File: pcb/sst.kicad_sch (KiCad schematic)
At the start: 24 parts

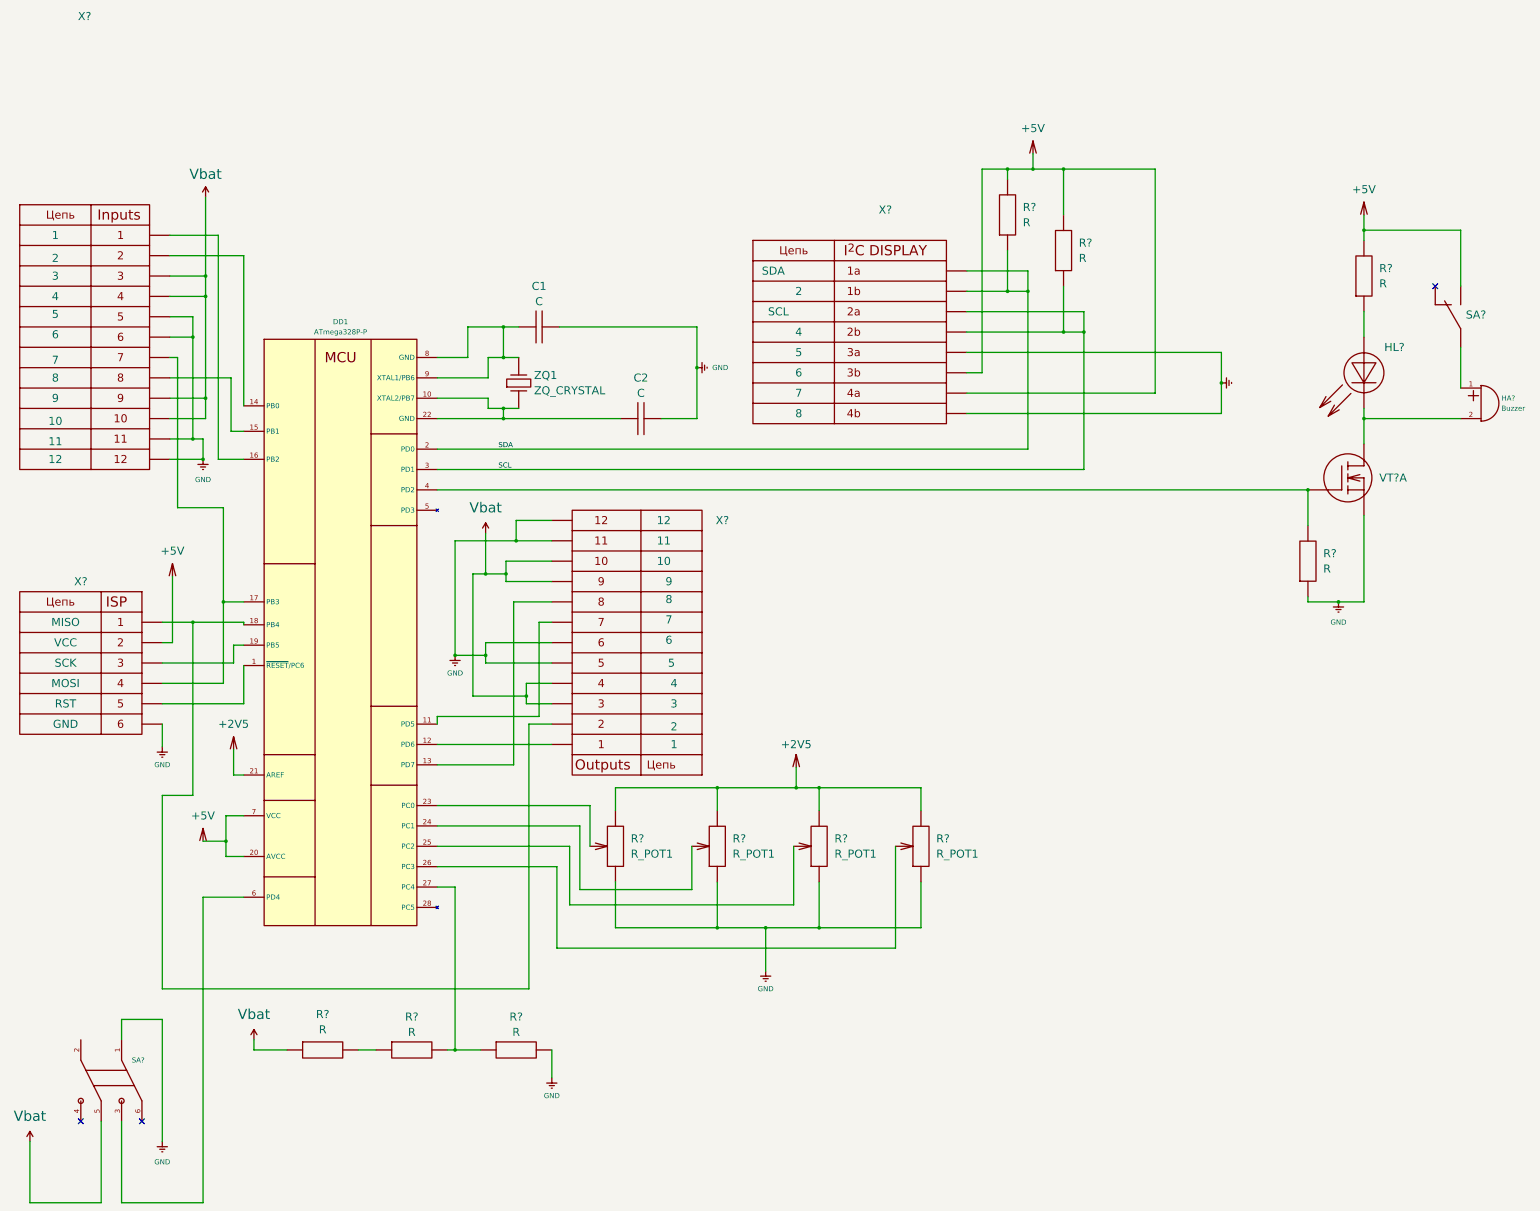
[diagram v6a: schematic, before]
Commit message: надпись «контакты» на уго
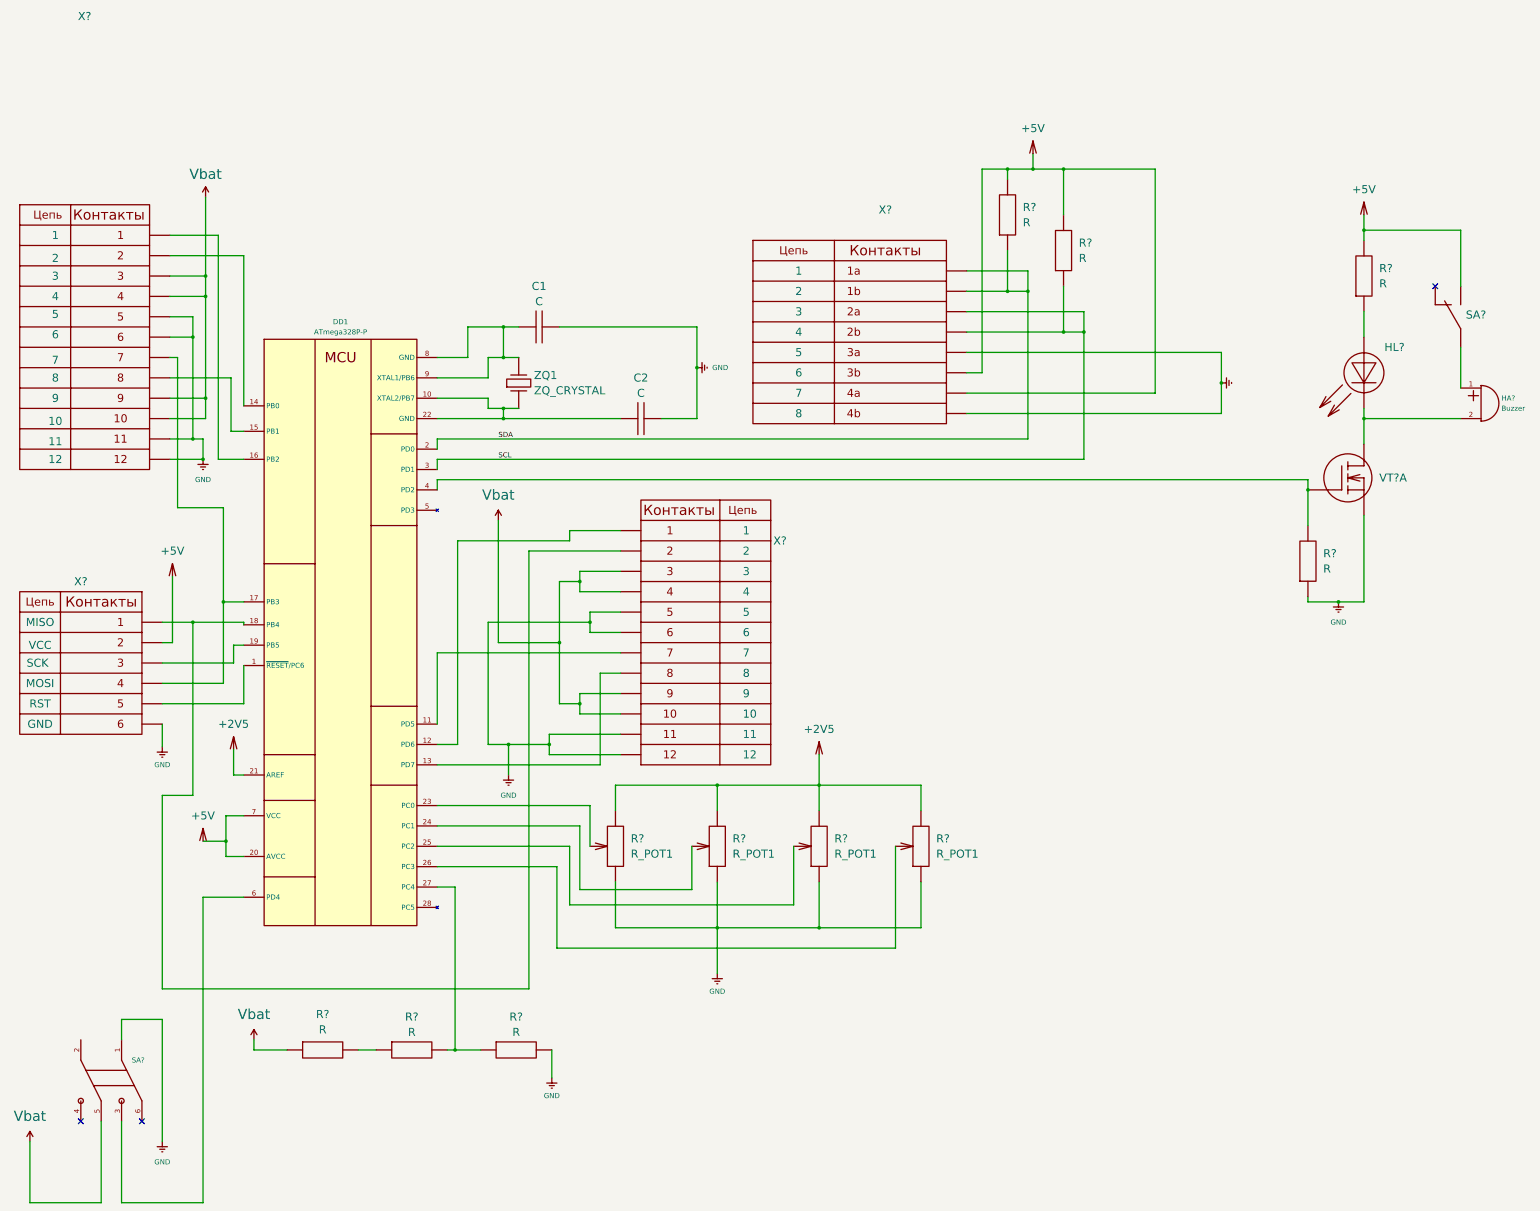
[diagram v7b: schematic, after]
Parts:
- removed X?: CONN_INPUTS, symbol sst:CONN_OUTPUTS
- added X?: CONN_INPUTS, symbol sst:CONN_OUTPUTS
- X?: PIN1 SDA -> 1; PIN3 SCL -> 3
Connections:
- net GND: now also X?.11, X?.12, X?.5, X?.6
- net Vbat: now also X?.10, X?.3, X?.4, X?.9
- net at DD1.11 (PD5): now also X?.7
- net at DD1.12 (PD6): now also X?.1
- net at DD1.13 (PD7): now also X?.8
- net at DD1.18 (PB4), X?.1: now also X?.2
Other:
- moved on the sheet: X?

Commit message: Символ земли без Value "GND"
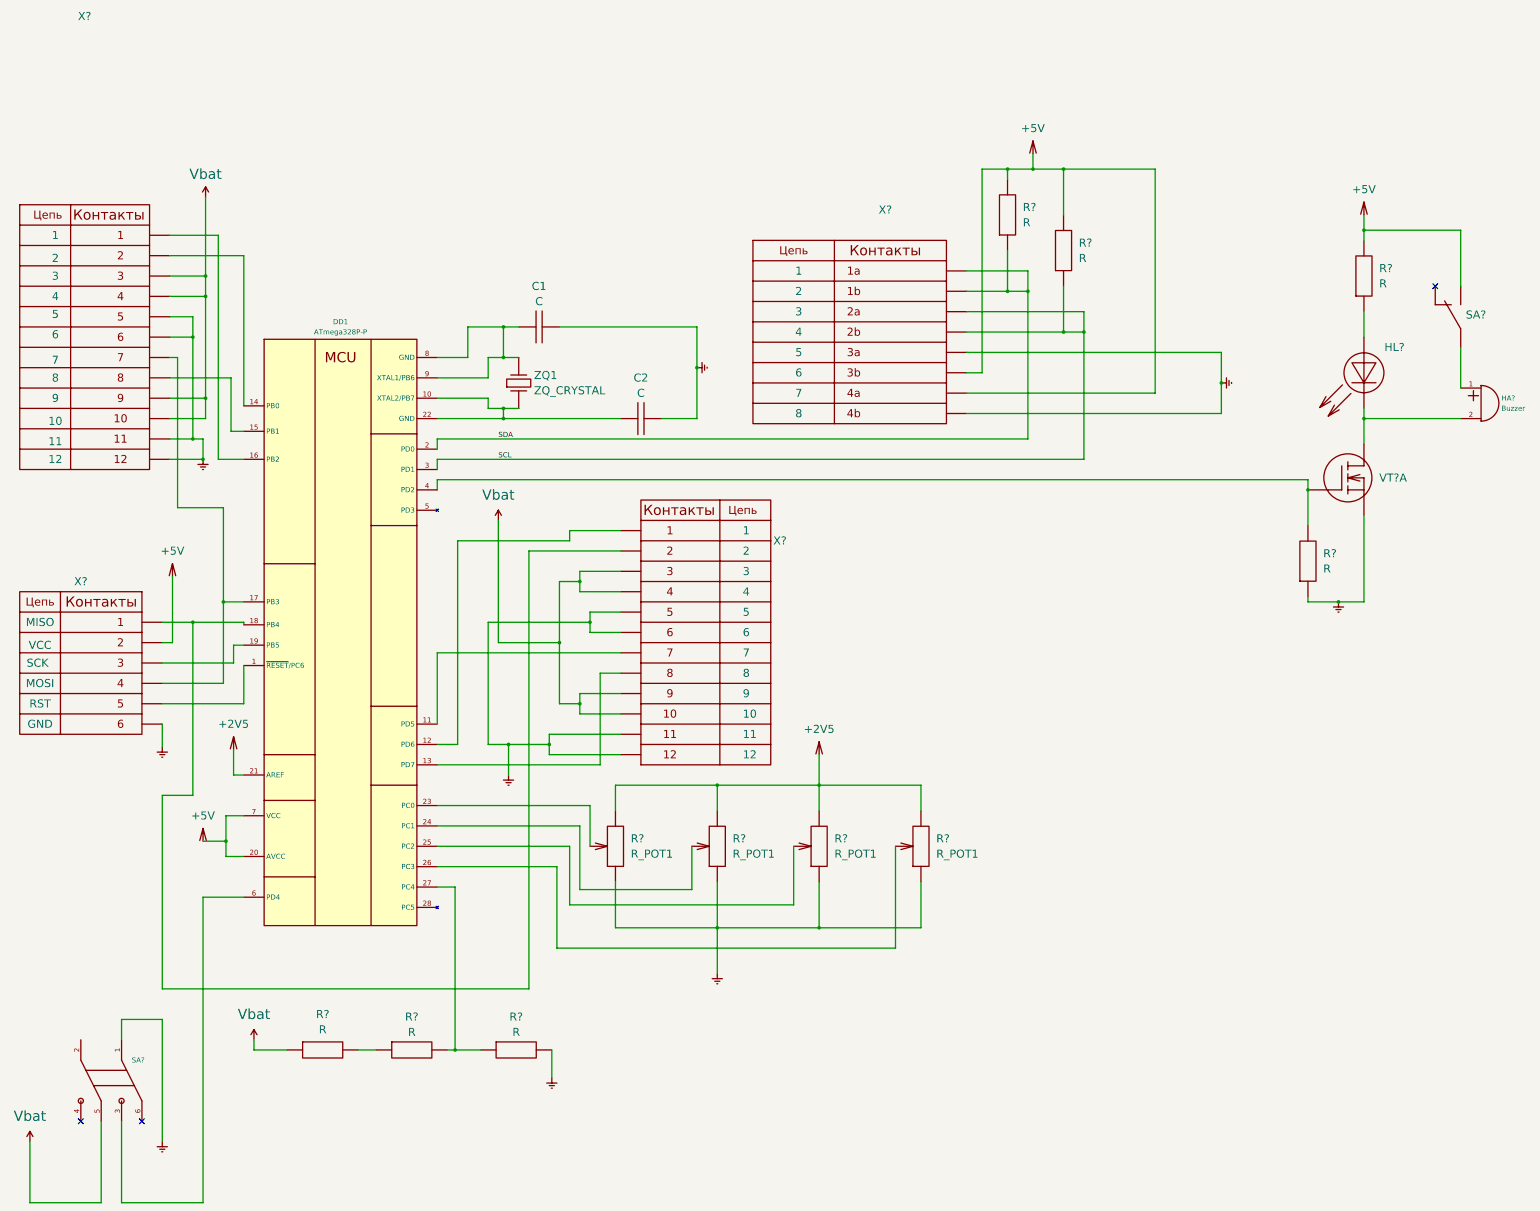
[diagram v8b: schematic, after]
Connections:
- removed net GND: C1.2, C2.1, R?.1, R?.1, R?.1, R?.1, R?.1, R?.2, SA?.1, VT?.1 (S1), X?.11, X?.11, X?.12, X?.12, X?.5, X?.5, X?.5, X?.6, X?.6, X?.6, X?.8
- new net: R?.1, R?.1, R?.1, R?.1
- new net: X?.11, X?.12, X?.5, X?.6 (x2)
- new net: X?.5, X?.8
- new net: C1.2, C2.1
- new net: R?.1, VT?.1 (S1)
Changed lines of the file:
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@@
 		(dnp no)
 		(fields_autoplaced yes)
-		(property "Reference" "#PWR015"
+		(property "Reference" "#PWR15"
 			(at 149.86 179.07 0)
 			(effects
@@
 			)
 		)
-		(property "Value" "GND"
-			(at 149.86 177.8 0)
+		(property "Value" ""
+			(at 149.86 176.53 0)
 			(effects
 				(font
@@
 			(project ""
 				(path "/d486a0a8-b0b2-426a-9635-bf463f56fa2d"
-					(reference "#PWR015")
+					(reference "#PWR15")
 					(unit 1)
 				)
@@
 		(dnp no)
 		(fields_autoplaced yes)
-		(property "Reference" "#PWR09"
+		(property "Reference" "#PWR9"
 			(at 73.66 100.33 0)
 			(effects
@@
 			)
 		)
-		(property "Value" "GND"
-			(at 73.66 99.06 0)
+		(property "Value" ""
+			(at 73.66 97.79 0)
 			(effects
 				(font
@@
 			(project ""
 				(path "/d486a0a8-b0b2-426a-9635-bf463f56fa2d"
-					(reference "#PWR09")
+					(reference "#PWR9")
 					(unit 1)
 				)
@@
 		(dnp no)
 		(fields_autoplaced yes)
-		(property "Reference" "#PWR01"
+		(property "Reference" "#PWR1"
 			(at 203.2 71.12 0)
 			(effects
@@
 			)
 		)
-		(property "Value" "GND"
-			(at 200.66 71.1199 90)
+		(property "Value" ""
+			(at 200.66 71.12 0)
 			(effects
 				(font
 					(size 1.27 1.27)
 				)
-				(justify right)
 			)
 		)
@@
 			(project ""
 				(path "/d486a0a8-b0b2-426a-9635-bf463f56fa2d"
-					(reference "#PWR01")
+					(reference "#PWR1")
 					(unit 1)
 				)
@@
 		(dnp no)
 		(fields_autoplaced yes)
-		(property "Reference" "#PWR07"
+		(property "Reference" "#PWR7"
 			(at 63.5 172.085 0)
 			(effects
@@
 			)
 		)
-		(property "Value" "GND"
-			(at 63.5 170.18 0)
+		(property "Value" ""
+			(at 63.5 169.545 0)
 			(effects
 				(font
@@
 			(project ""
 				(path "/d486a0a8-b0b2-426a-9635-bf463f56fa2d"
-					(reference "#PWR07")
+					(reference "#PWR7")
 					(unit 1)
 				)
@@
 		(dnp no)
 		(fields_autoplaced yes)
-		(property "Reference" "#PWR02"
+		(property "Reference" "#PWR2"
 			(at 334.01 74.93 0)
 			(effects
@@
 			)
 		)
-		(property "Value" "GND"
-			(at 331.47 74.9299 90)
+		(property "Value" ""
+			(at 331.47 74.93 0)
 			(effects
 				(font
 					(size 1.27 1.27)
 				)
-				(justify right)
-				(hide yes)
 			)
 		)
@@
 			(project ""
 				(path "/d486a0a8-b0b2-426a-9635-bf463f56fa2d"
-					(reference "#PWR02")
+					(reference "#PWR2")
 					(unit 1)
 				)
@@
 		(dnp no)
 		(fields_autoplaced yes)
-		(property "Reference" "#PWR04"
+		(property "Reference" "#PWR4"
 			(at 356.87 135.89 0)
 			(effects
@@
 			)
 		)
-		(property "Value" "GND"
-			(at 356.87 134.62 0)
+		(property "Value" ""
+			(at 356.87 133.35 0)
 			(effects
 				(font
@@
 			(project ""
 				(path "/d486a0a8-b0b2-426a-9635-bf463f56fa2d"
-					(reference "#PWR04")
+					(reference "#PWR4")
 					(unit 1)
 				)
@@
 		(dnp no)
 		(fields_autoplaced yes)
-		(property "Reference" "#PWR018"
+		(property "Reference" "#PWR18"
 			(at 63.5 270.51 0)
 			(effects
@@
 			)
 		)
-		(property "Value" "GND"
-			(at 63.5 269.24 0)
+		(property "Value" ""
+			(at 63.5 267.97 0)
 			(effects
 				(font
@@
 			(project ""
 				(path "/d486a0a8-b0b2-426a-9635-bf463f56fa2d"
-					(reference "#PWR018")
+					(reference "#PWR18")
 					(unit 1)
 				)
@@
 		(dnp no)
 		(fields_autoplaced yes)
-		(property "Reference" "#PWR014"
+		(property "Reference" "#PWR14"
 			(at 201.93 228.6 0)
 			(effects
@@
 			)
 		)
-		(property "Value" "GND"
-			(at 201.93 226.695 0)
+		(property "Value" ""
+			(at 201.93 226.06 0)
 			(effects
 				(font
@@
 			(project ""
 				(path "/d486a0a8-b0b2-426a-9635-bf463f56fa2d"
-					(reference "#PWR014")
+					(reference "#PWR14")
 					(unit 1)
 				)
@@
 		(dnp no)
 		(fields_autoplaced yes)
-		(property "Reference" "#PWR017"
+		(property "Reference" "#PWR17"
 			(at 160.655 254.635 0)
 			(effects
@@
 			)
 		)
-		(property "Value" "GND"
-			(at 160.655 252.73 0)
+		(property "Value" ""
+			(at 160.655 252.095 0)
 			(effects
 				(font
@@
 			(project ""
 				(path "/d486a0a8-b0b2-426a-9635-bf463f56fa2d"
-					(reference "#PWR017")
+					(reference "#PWR17")
 					(unit 1)
 				)
